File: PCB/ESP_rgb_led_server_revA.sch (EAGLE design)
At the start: 33 parts, among them U1 AMS1117, U2 ESP-12F

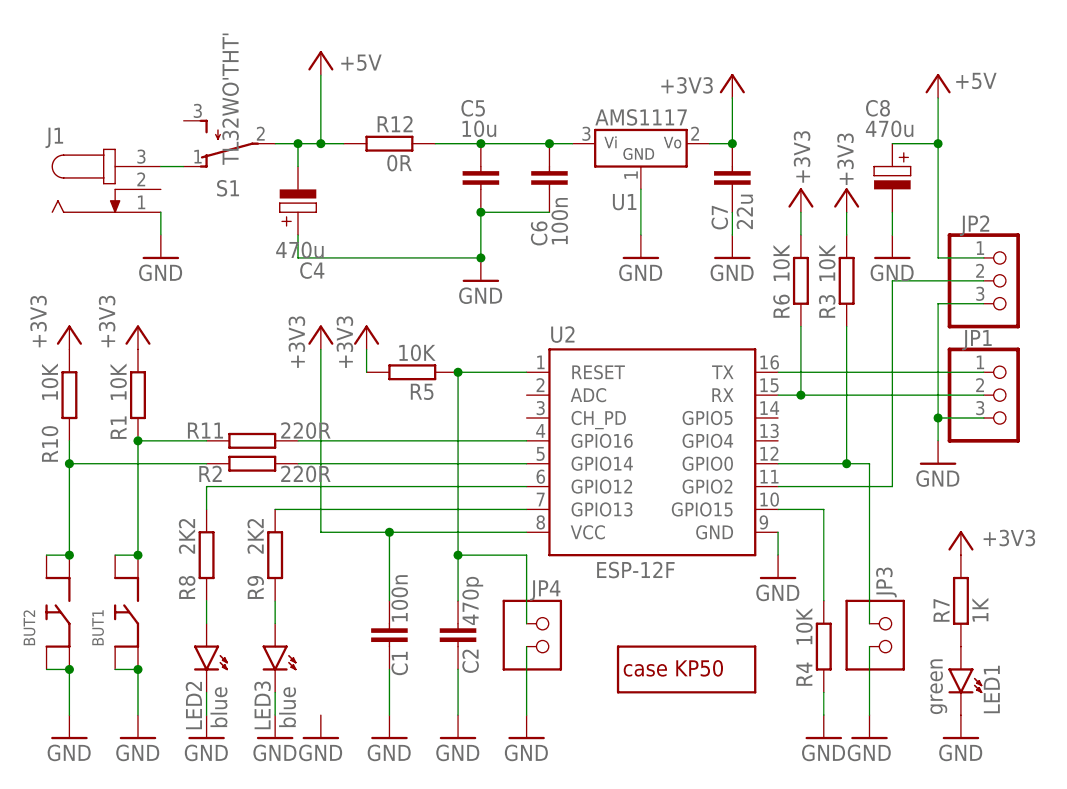
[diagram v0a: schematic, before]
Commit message: added: schematics and layout exported as images
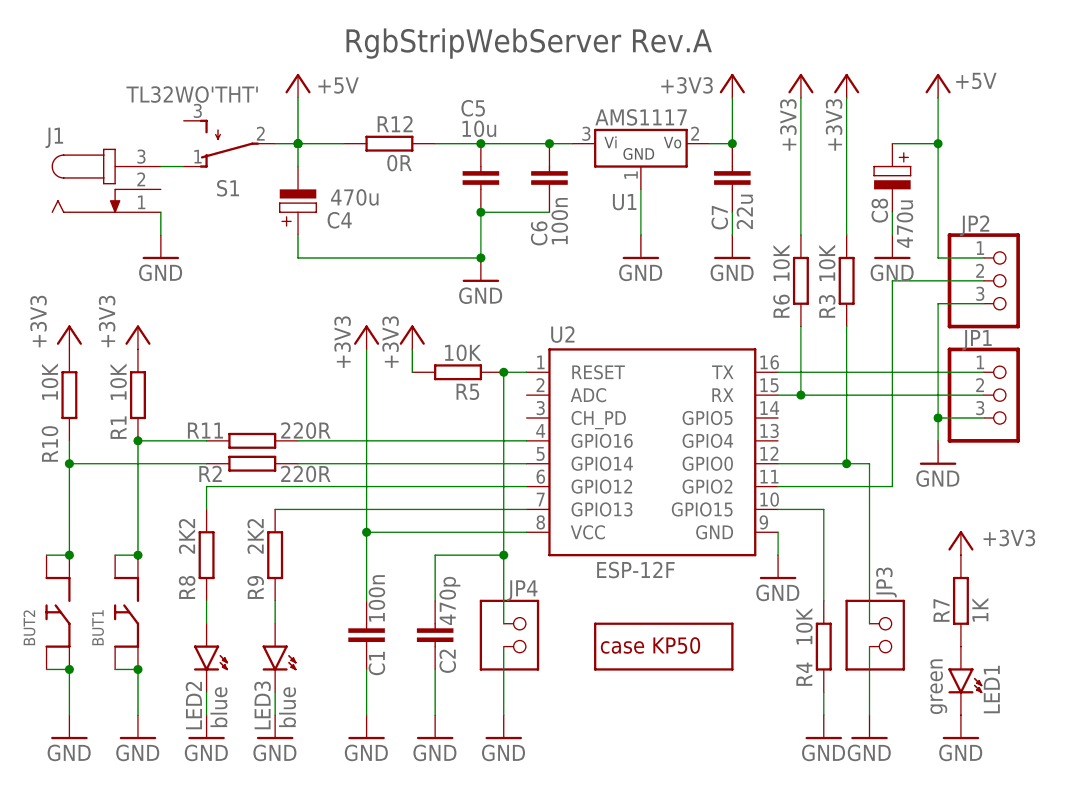
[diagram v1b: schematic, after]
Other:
- note added: "RgbStripWebServer Rev.A"
- moved on the sheet: C1, C2, JP4, R5
